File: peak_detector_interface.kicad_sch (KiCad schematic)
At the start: 11 parts

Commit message: some changes after first test of boards. Package of SN74LV221AD changed to SOIC-16.
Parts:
- C600, C601: JLCplace (none) -> C1710; Supplier (none) -> LCSC
- JP600, JP601, JP602, JP603, JP604, JP605, TP17: Supplier (none) -> --
- R600: JLCplace (none) -> C17414; Supplier (none) -> LCSC
- R601: JLCplace (none) -> C17513; Supplier (none) -> LCSC
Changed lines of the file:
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@@
+      (effects (font (size 1.27 1.27)) hide)
+    )
+    (property "Supplier" "--" (id 4) (at 182.88 63.5 0)
       (effects (font (size 1.27 1.27)) hide)
     )
@@
       (effects (font (size 1.27 1.27)) hide)
     )
+    (property "Supplier" "--" (id 4) (at 81.28 67.31 0)
+      (effects (font (size 1.27 1.27)) hide)
+    )
     (pin "1")
     (pin "2")
@@
       (effects (font (size 1.27 1.27)) hide)
     )
+    (property "Supplier" "--" (id 4) (at 116.84 60.96 0)
+      (effects (font (size 1.27 1.27)) hide)
+    )
     (pin "1")
     (pin "2")
@@
       (effects (font (size 1.27 1.27)) hide)
     )
+    (property "Supplier" "--" (id 4) (at 152.4 60.96 0)
+      (effects (font (size 1.27 1.27)) hide)
+    )
     (pin "1")
     (pin "2")
@@
       (effects (font (size 1.27 1.27)) hide)
     )
+    (property "Supplier" "--" (id 4) (at 191.77 68.58 0)
+      (effects (font (size 1.27 1.27)) hide)
+    )
     (pin "1")
     (pin "2")
@@
     )
     (property "OriginalType" "WR08X1002FTL" (id 7) (at 91.44 73.66 0)
+      (effects (font (size 1.27 1.27)) hide)
+    )
+    (property "Supplier" "LCSC" (id 8) (at 91.44 73.66 0)
+      (effects (font (size 1.27 1.27)) hide)
+    )
+    (property "JLCplace" "C17414" (id 9) (at 91.44 73.66 0)
       (effects (font (size 1.27 1.27)) hide)
     )
@@
       (effects (font (size 1.27 1.27)) hide)
     )
+    (property "Supplier" "LCSC" (id 8) (at 175.26 68.58 0)
+      (effects (font (size 1.27 1.27)) hide)
+    )
+    (property "JLCplace" "C17513" (id 9) (at 175.26 68.58 0)
+      (effects (font (size 1.27 1.27)) hide)
+    )
     (pin "1")
     (pin "2")
@@
       (effects (font (size 1.27 1.27)) hide)
     )
+    (property "Supplier" "LCSC" (id 8) (at 99.06 67.31 0)
+      (effects (font (size 1.27 1.27)) hide)
+    )
+    (property "JLCplace" "C1710" (id 9) (at 99.06 67.31 0)
+      (effects (font (size 1.27 1.27)) hide)
+    )
     (pin "1")
     (pin "2")
@@
       (effects (font (size 1.27 1.27)) hide)
     )
+    (property "Supplier" "LCSC" (id 8) (at 182.88 76.2 0)
+      (effects (font (size 1.27 1.27)) hide)
+    )
+    (property "JLCplace" "C1710" (id 9) (at 182.88 76.2 0)
+      (effects (font (size 1.27 1.27)) hide)
+    )
     (pin "1")
     (pin "2")
@@
       (effects (font (size 1.27 1.27)) hide)
     )
+    (property "Supplier" "--" (id 4) (at 114.3 50.8 0)
+      (effects (font (size 1.27 1.27)) hide)
+    )
     (pin "1")
     (pin "2")
@@
       (effects (font (size 1.27 1.27)) hide)
     )
+    (property "Supplier" "--" (id 4) (at 157.48 50.8 0)
+      (effects (font (size 1.27 1.27)) hide)
+    )

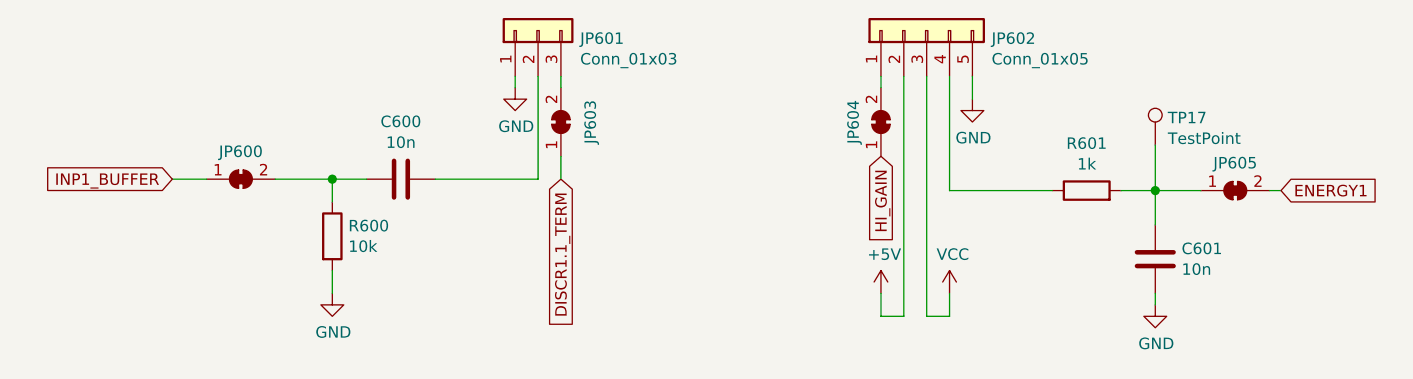
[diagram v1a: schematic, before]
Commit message: KiCad update to 6.0.0-rc1-114-gb471945224
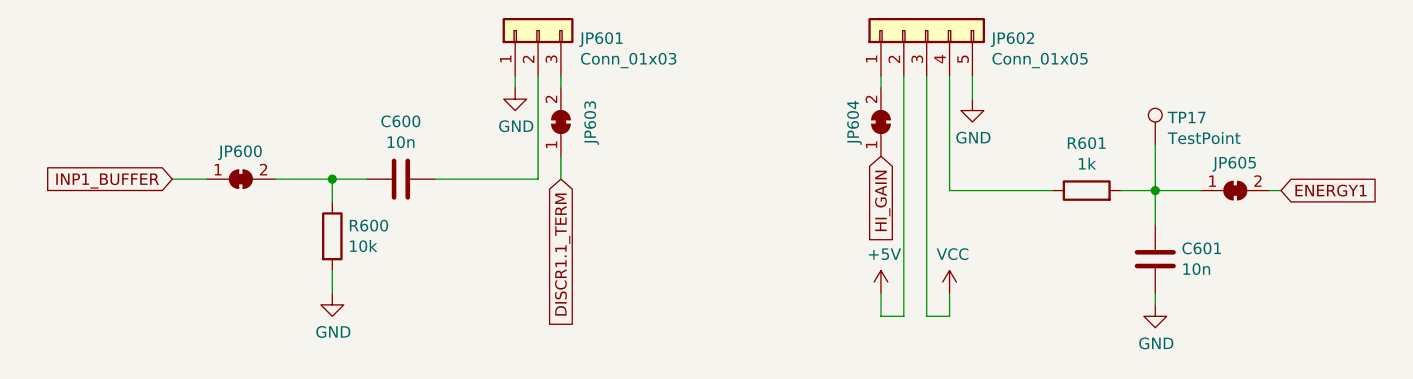
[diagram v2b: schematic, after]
